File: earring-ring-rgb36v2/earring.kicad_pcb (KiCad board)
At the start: 2 copper layers, 75 x 92.5 mm, 67 parts, among them J1 Conn_01x05, Q1 AO3401A, Q2 Q_Photo_NPN_EC, SW1 SW_Push, SW2 SW_Push, U1 GMA2718H09-F42-4P, U2 STM32L031G6Ux, Y1 Crystal

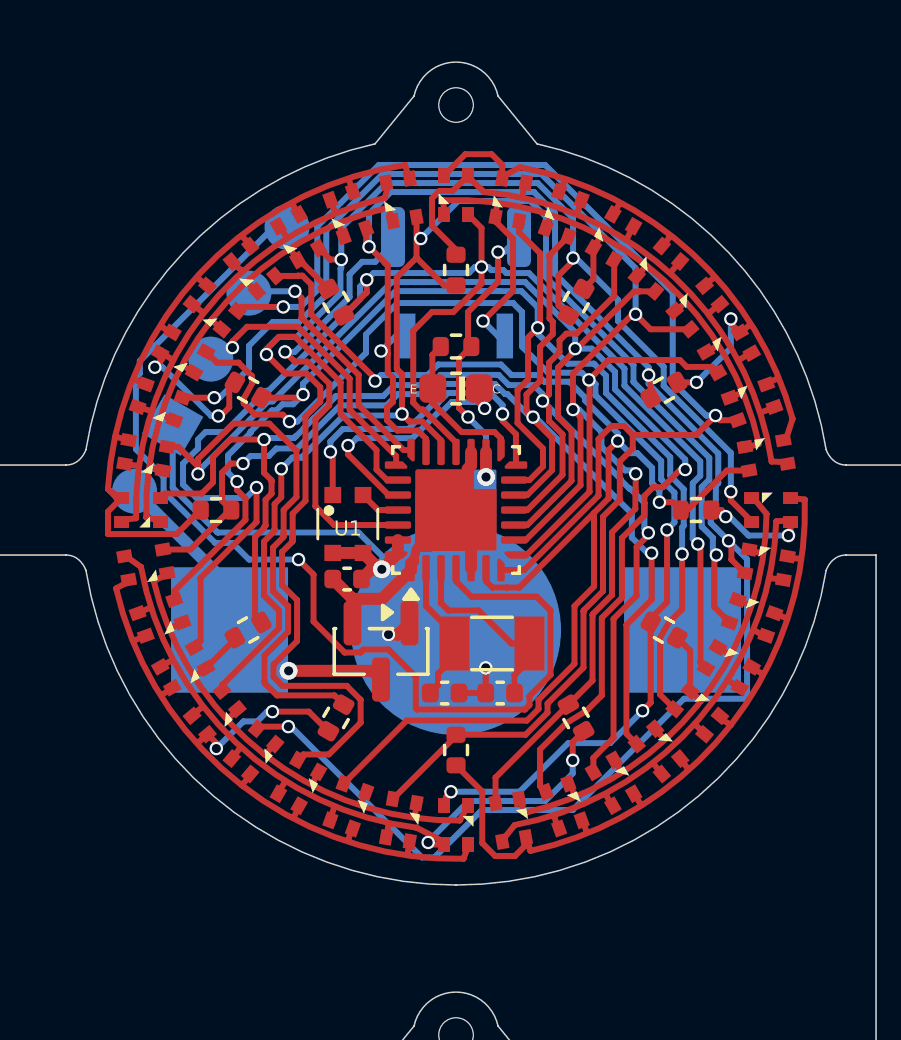
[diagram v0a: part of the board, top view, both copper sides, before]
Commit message: earring-ring-rgb36v2: many changes for next prototype
* remove crystal
* remove light sensor
* add extra button
* add capacitor to VDDA and to the microphone
* move capacitor to above the chip
* many small changes to make the design look a bit more symmetric
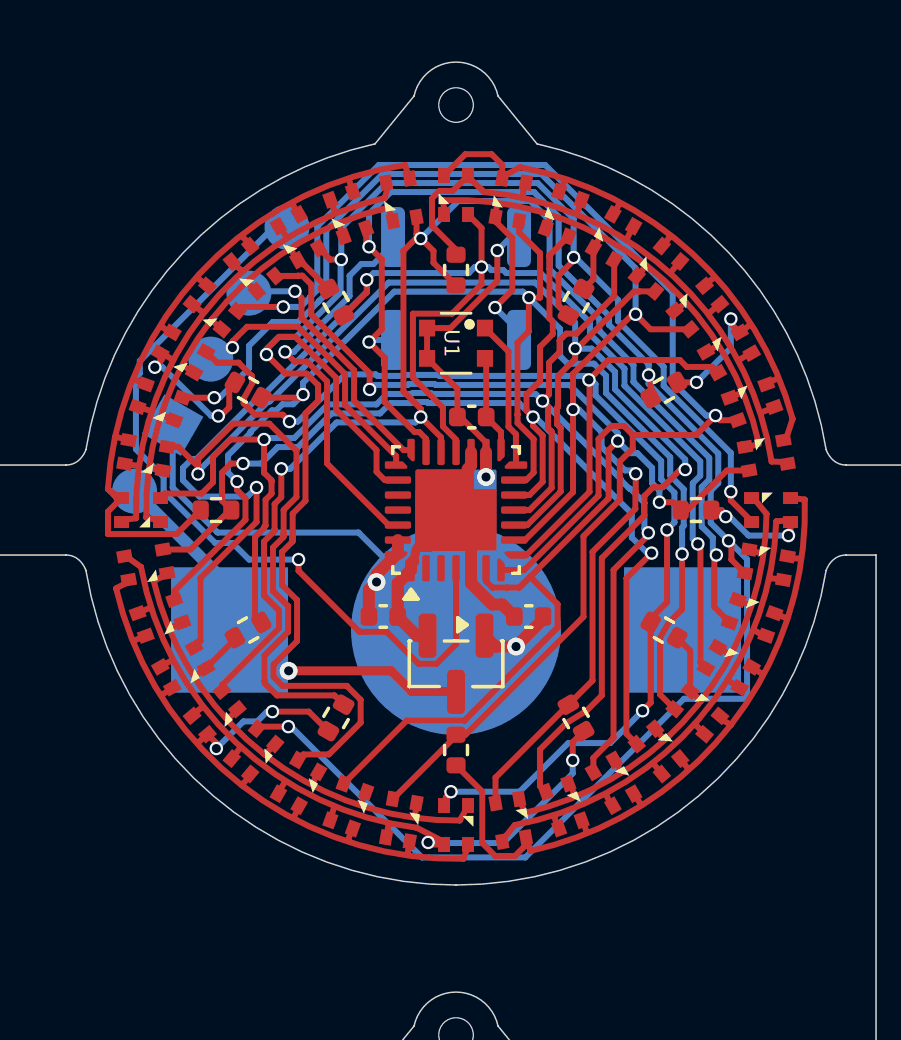
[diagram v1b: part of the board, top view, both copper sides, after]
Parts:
- removed Q2: Q_Photo_NPN_EC, Custom:Phototransistor_0603
- removed R13: 10k, Resistor_SMD:R_0402_1005Metric
- removed Y1: Crystal, Crystal:Crystal_SMD_3215-2Pin_3.2x1.5mm
- C2, C3: value 22pF -> 0.1uF
- SW2: footprint Custom:KXT311LHS -> Button_Switch_SMD:SW_Push_SPST_NO_Alps_SKRK
- moved C2 9.24 mm to (0.53, -3.10)
- moved U1 7.02 mm to (0.00, -5.56), turned to -90 degrees
- moved C3 2.72 mm to (2.42, 3.55)
- moved Q1 2.53 mm to (0.00, 5.12)
- moved C1 1.74 mm to (-2.42, 3.55), turned to 180 degrees
- moved SW2 0.13 mm to (0.00, -5.67)
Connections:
- C2 pad 1: GND -> MIC_VCC
- C2 pad 2: Net-(U2-PC14) -> GND
- C3 pad 1: GND -> VCC
- C3 pad 2: Net-(U2-PC15) -> GND
- U2 pad 15: PHOTO_SENSE -> MIC_VCC
- U2 pad 2: Net-(U2-PC14) -> unconnected-(U2-PC14-Pad2)
- U2 pad 24: PHOTO_VCC -> unconnected-(U2-PB3-Pad24)
- U2 pad 25: MIC_VCC -> unconnected-(U2-PB6-Pad25)
- U2 pad 3: Net-(U2-PC15) -> unconnected-(U2-PC15-Pad3)
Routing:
- net NRST: track 35.9 -> 26.7 mm
- net PHOTO_VCC: track 8.57 -> 0.00 mm, vias 2 -> 0
- net Net-(U2-PC15): track 6.53 -> 0.00 mm
- net MIC_SENSE: track 10.6 -> 4.99 mm, vias 2 -> 0
- net PHOTO_SENSE: track 5.16 -> 0.00 mm
- net Net-(U2-PC14): track 4.89 -> 0.00 mm
- net A12: track 44.1 -> 40.6 mm
- net A10: track 50.3 -> 47.3 mm
- net VBAT: track 11.5 -> 14.1 mm
- net MIC_VCC: track 1.37 -> 3.28 mm
- net Net-(U2-PB7): track 15.6 -> 14.1 mm
- net VCC: track 8.89 -> 10.2 mm
- net A11: track 52.7 -> 51.5 mm
- net A7: track 47.3 -> 46.4 mm
- net A3: track 45.3 -> 46.0 mm
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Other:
- board text added: "v1.2"
- board text removed: "v1.1b"

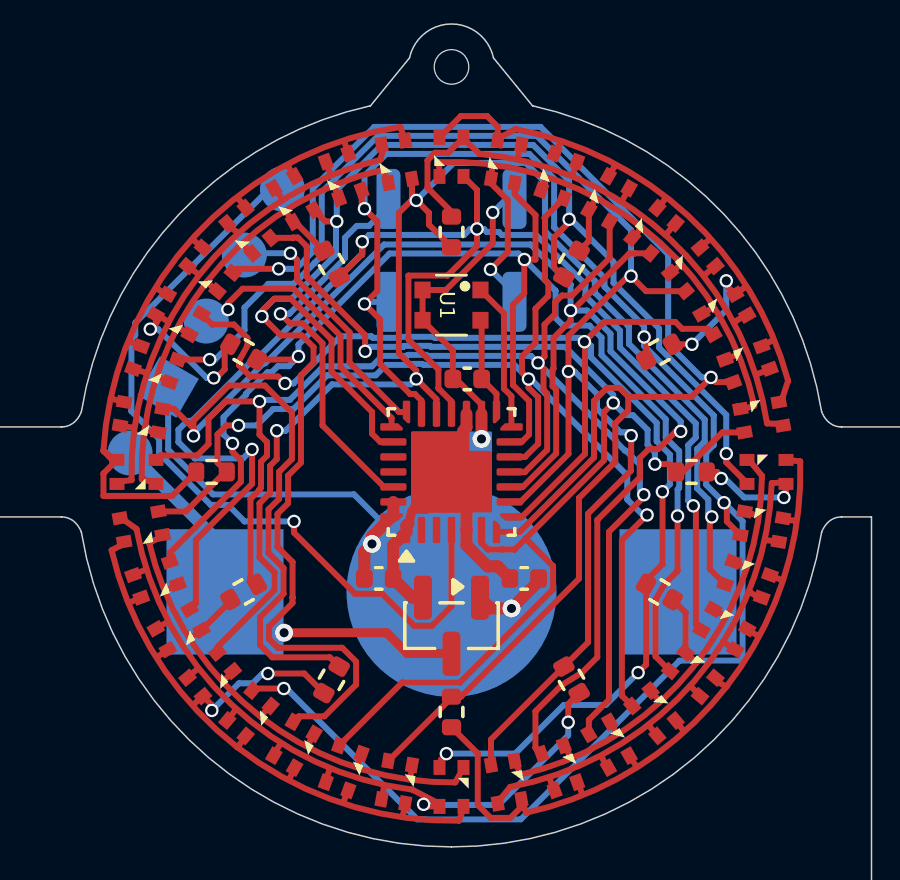
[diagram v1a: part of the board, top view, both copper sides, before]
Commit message: earring-ring-rgb36v6: small modifications to clean up the PCB
Should be ready for test production now.
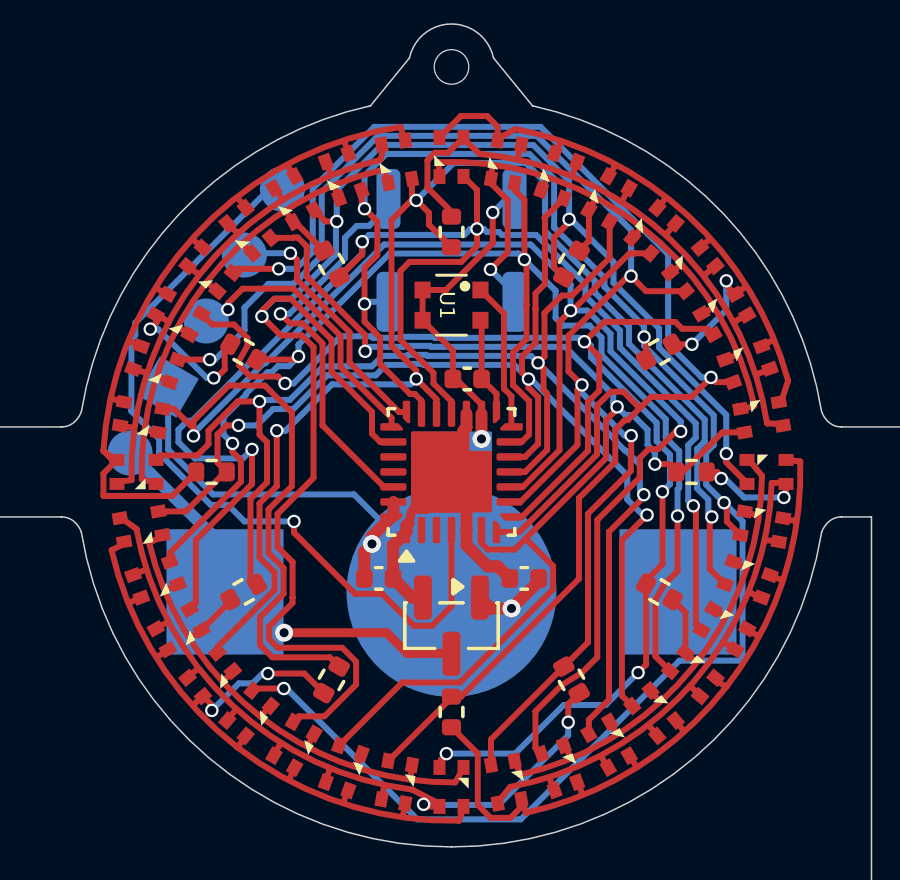
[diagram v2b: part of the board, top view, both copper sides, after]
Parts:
- SW1, SW2: footprint Button_Switch_SMD:SW_Push_SPST_NO_Alps_SKRK -> Custom:SW_Push_SPST_NO_Alps_SKRK

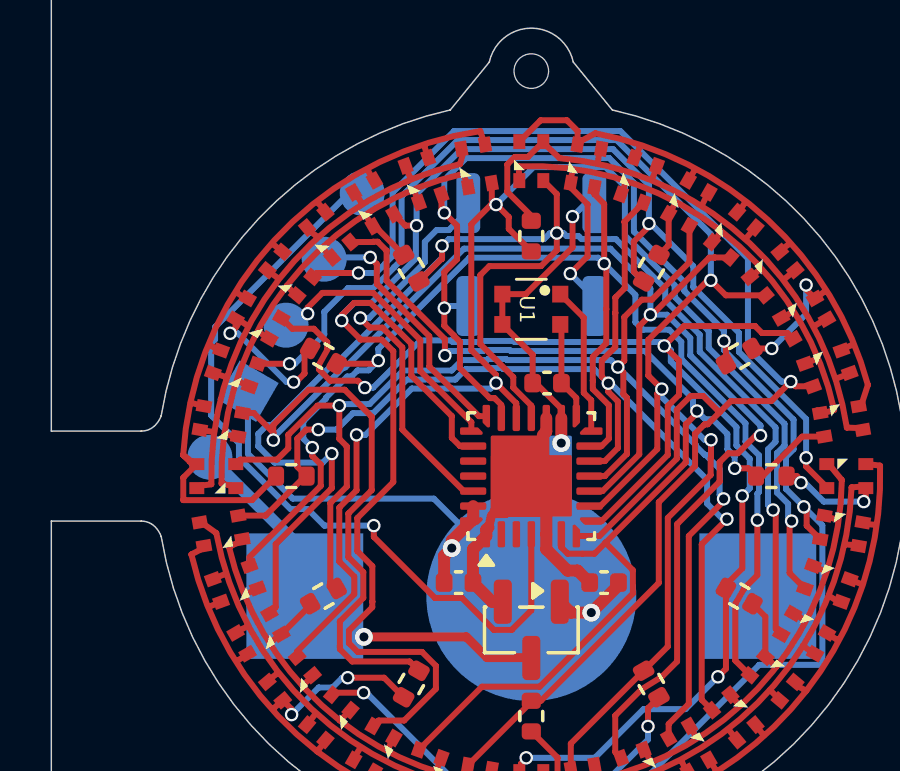
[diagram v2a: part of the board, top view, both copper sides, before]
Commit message: earring-ring-rgb36v2: fix 2nd button wiring
Previous wiring wasn't correct: pressing the button would make some LEDs
light up that shouldn't while charlieplexing.
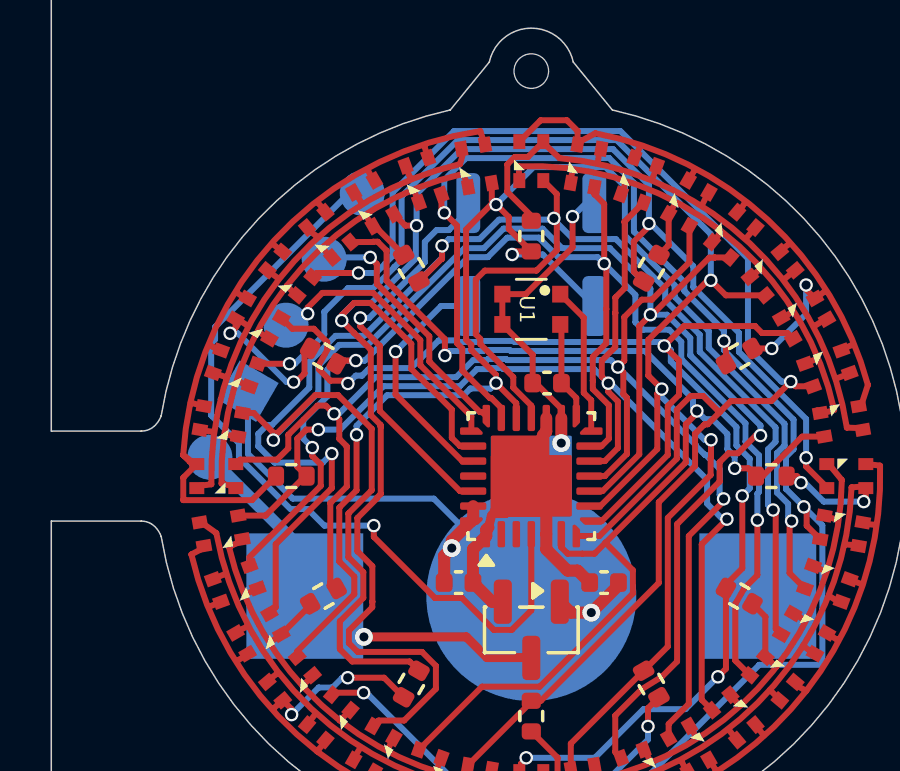
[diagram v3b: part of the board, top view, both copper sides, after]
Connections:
- SW2 pad 1: A1R -> A3
- SW2 pad 2: A2 -> Net-(U2-PB3)
- U2 pad 24: unconnected-(U2-PB3-Pad24) -> Net-(U2-PB3)
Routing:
- net Net-(U2-PB3): track 0.00 -> 7.99 mm, vias 0 -> 1
- net A1R: track 6.53 -> 1.63 mm, vias 1 -> 0
- net A3: track 46.2 -> 50.7 mm, vias 4 -> 5
- net A2: track 58.9 -> 57.7 mm, vias 5 -> 4
- net A4: track 52.5 -> 53.6 mm
- net A1: track 57.5 -> 56.7 mm

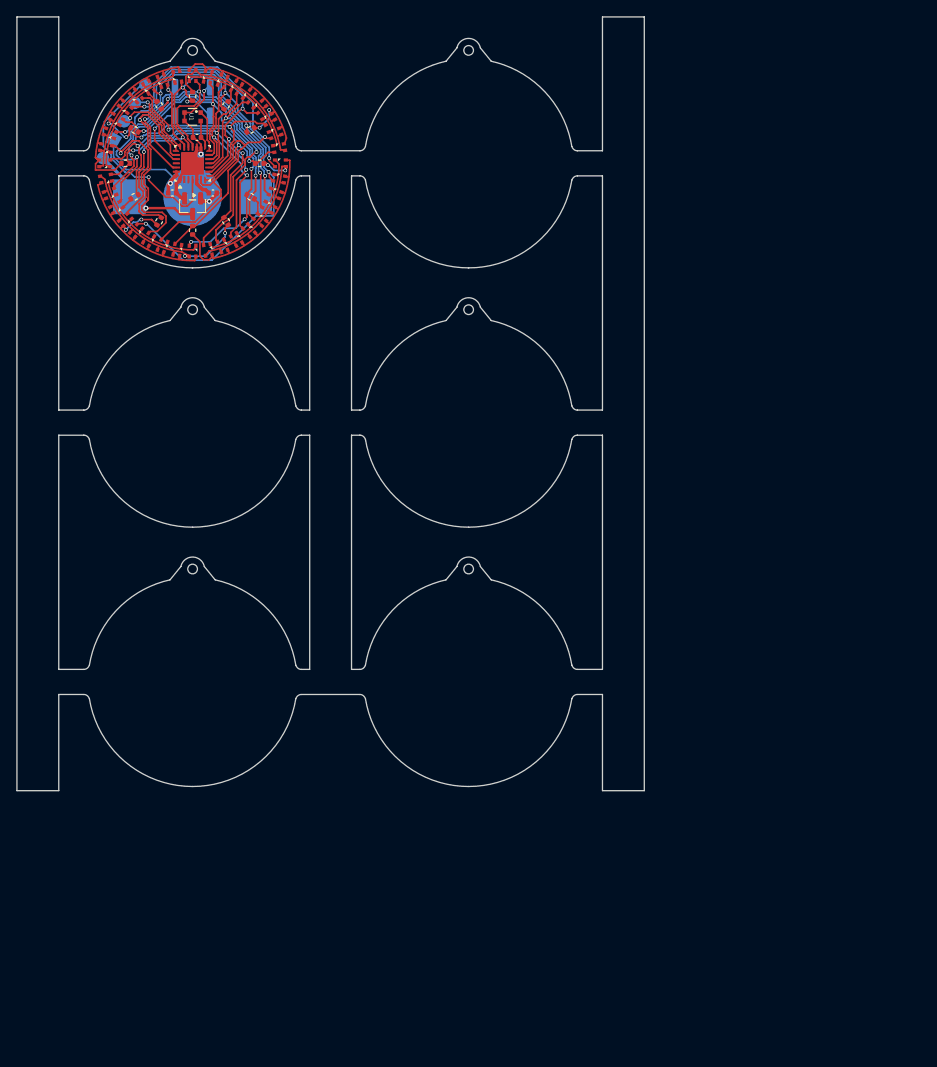
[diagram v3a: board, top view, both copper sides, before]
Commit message: earring-ring-rgb36v2: extend PCB panel to 3x4 PCBs
This increases the boards per panel from 6 to 12, which makes handling a
bit easier and allows for larger order sizes (with the prototyping
service that is limited to 30 panels).
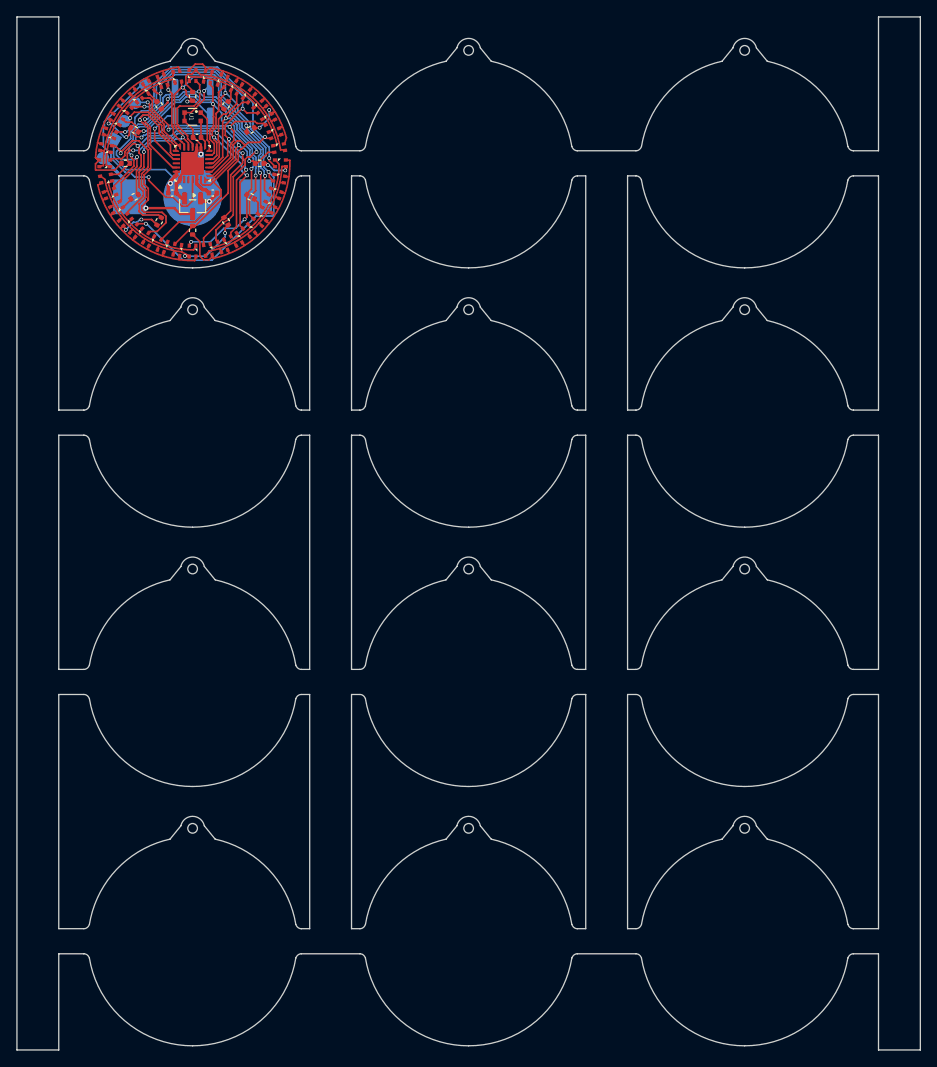
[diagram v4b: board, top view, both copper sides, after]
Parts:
- added H1: ToolingHole, Custom:ToolingHole_JLCPCB, F.Cu at (66.0, 17.5)
- added H1: ToolingHole, Custom:ToolingHole_JLCPCB, F.Cu at (33.0, 79.5)
- added H1: ToolingHole, Custom:ToolingHole_JLCPCB, F.Cu at (66.0, 79.5)
- added H1: ToolingHole, Custom:ToolingHole_JLCPCB, F.Cu at (0.00, 79.5)
- added H1: ToolingHole, Custom:ToolingHole_JLCPCB, F.Cu at (66.0, -13.5)
- added H1: ToolingHole, Custom:ToolingHole_JLCPCB, F.Cu at (66.0, 48.5)
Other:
- board size 75 x 92.5 mm -> 108 x 123.5 mm

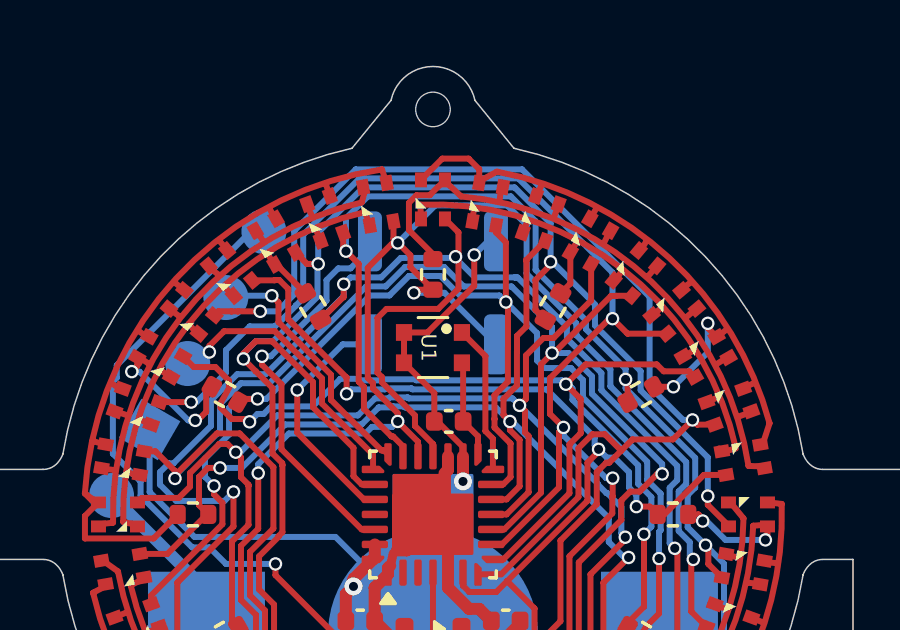
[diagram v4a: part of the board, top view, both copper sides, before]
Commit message: earring-ring-rgb36v2: change wiring slightly to be more sensible
The button had some weird wiring, it makes much more sense to connect
the button between a pin and ground.
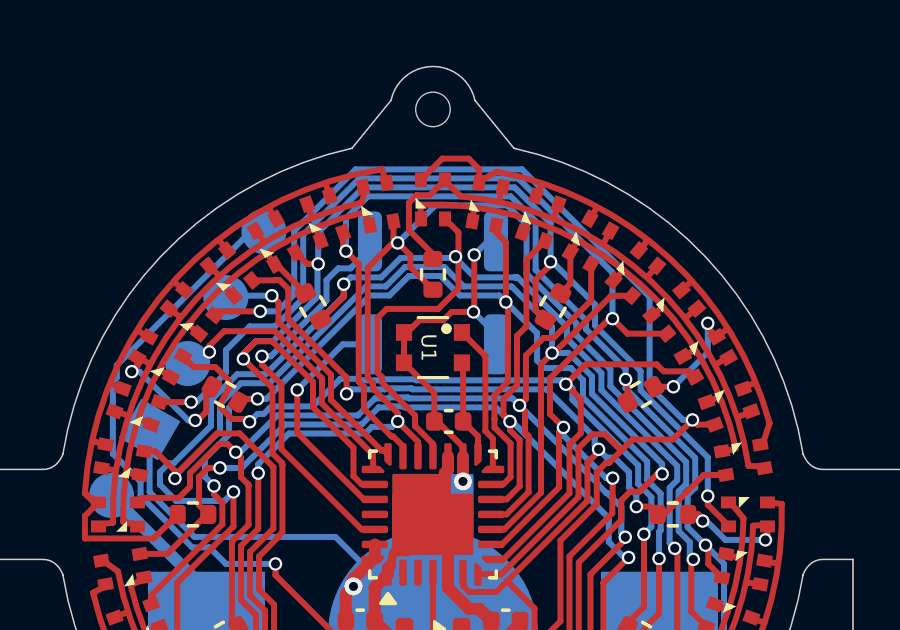
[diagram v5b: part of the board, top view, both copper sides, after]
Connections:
- SW2 pad 1: A3 -> GND
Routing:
- net A3: track 50.7 -> 46.5 mm, vias 5 -> 4
- net GND: track 34.3 -> 36.2 mm, vias 4 -> 5

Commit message: earring-ring-rgb36v2: update silkscreen for production
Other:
- board text added: "v2.0"
- board text added: "variant"
- board text removed: "color/ program"
- board text removed: "v1.2"
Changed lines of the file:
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@@
 	)
 	(gr_line
-		(start 2.7 -5.85)
-		(end 3 -6.15)
+		(start 2.7 -5.65)
+		(end 3 -5.95)
 		(stroke
 			(width 0.15)
@@
 	)
 	(gr_line
-		(start 2.7 -5.85)
-		(end 3 -5.55)
+		(start 2.7 -5.65)
+		(end 3 -5.35)
 		(stroke
 			(width 0.15)
@@
 	)
 	(gr_line
-		(start 2.7 -5.85)
-		(end 4.4 -5.85)
+		(start 2.7 -5.65)
+		(end 4.55 -5.65)
 		(stroke
 			(width 0.15)
@@
 	)
 	(gr_line
-		(start 4.4 -5.85)
-		(end 4.4 -5.35)
+		(start 4.55 -5.65)
+		(end 4.55 -4.725)
 		(stroke
 			(width 0.15)
@@
 		)
 	)
-	(gr_text "color/\nprogram"
-		(at 6.6 -3.3 0)
+	(gr_text "variant"
+		(at 6.85 -3.325 0)
 		(layer "B.SilkS")
 		(effects
 			(font
-				(size 0.75 0.75)
+				(size 0.85 0.85)
 				(thickness 0.15)
 			)
@@
 	)
 	(gr_text "LED earring"
-		(at 7.7 -4 312)
+		(at 7.6 -3.925 312)
 		(layer "B.SilkS")
 		(effects
@@
 		)
 	)
-	(gr_text "v1.2"
+	(gr_text "v2.0"
 		(at 5.325 0.875 315)
 		(layer "B.SilkS")
